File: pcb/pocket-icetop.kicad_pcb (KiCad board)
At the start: 2 copper layers, 100 x 50 mm, 39 parts, among them CON1 5V_DC, P1 USB_B, P2 LED_POWER, P3 ICSP, P4 LED_STRIP, SW1 RESET, SW2 SW_DEMO1, SW3 SW_DEMO2, U1 ATMEGA32U4-A, Y1 Crystal

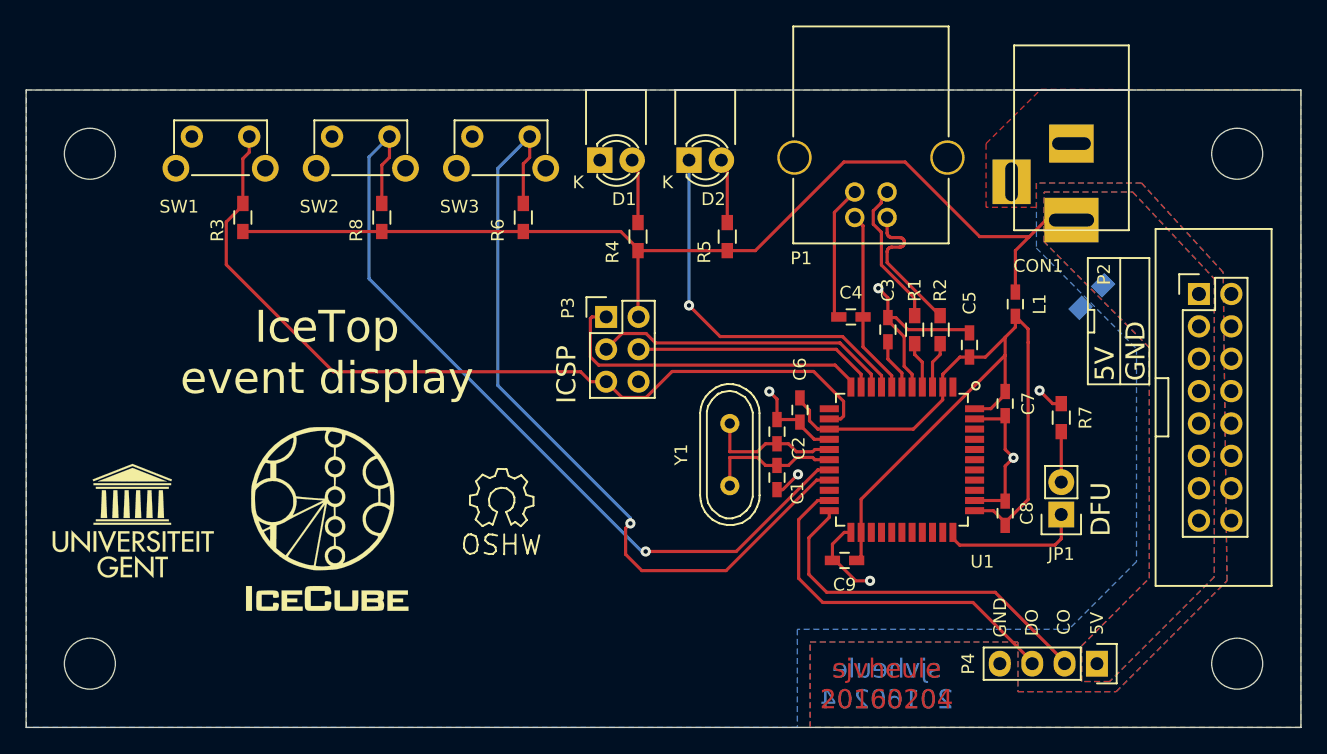
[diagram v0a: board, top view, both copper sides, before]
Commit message: Drop DFU jumper by using SW3 as dual-purpose input: demo button and DFU select during reset.
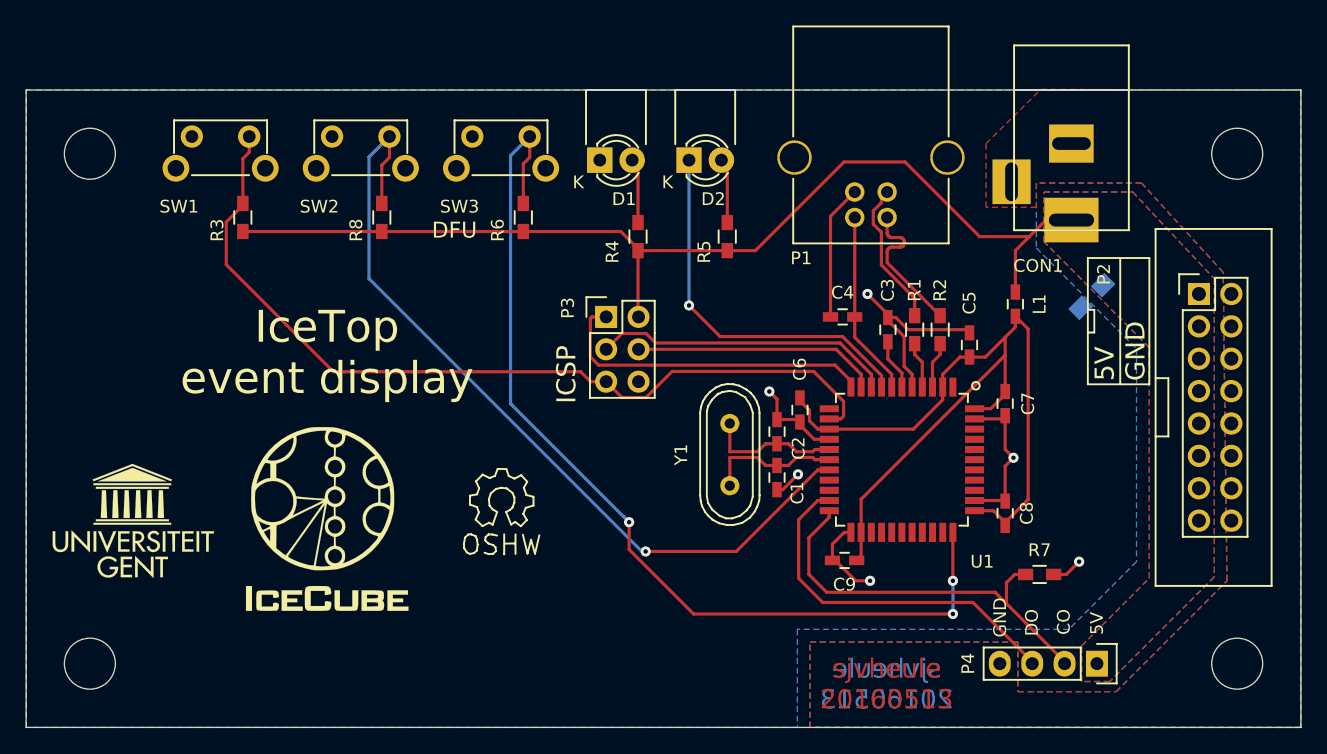
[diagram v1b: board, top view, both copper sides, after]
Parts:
- removed JP1: JUMPER, Pin_Headers:Pin_Header_Straight_1x02
- C1, C2: value 6p -> 6.8p
- U1: value ATMEGA32U4-A -> ATMEGA32U4-AU
- moved R7 12.4 mm to (121.5, 80.0), turned to 0 degrees
- moved C4 0.65 mm to (106.0, 59.8)
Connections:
- R7 pad 1: GND -> LED_clk
- R7 pad 2: Net-(JP1-Pad2) -> GND
- U1 pad 19: /DEMO2 -> Net-(U1-Pad19)
- U1 pad 33: Net-(JP1-Pad1) -> /DEMO2
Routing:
- net /DEMO2: track 63.2 -> 76.7 mm, vias 1 -> 3
- net Net-(JP1-Pad1): track 11.3 -> 0.00 mm
- net Net-(JP1-Pad2): track 3.96 -> 0.00 mm
- net LED_clk: track 28.7 -> 32.1 mm
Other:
- board text added: "Rev 2: Update DC jack footprint, move copper fills accordingly Rev 3: Move C4 to make room for C3's marking by moving C3's GND via Add pull-down to LED clock line Replace DFU jumper by SW3"
- board text added: "sjvheule 20160513"
- board text removed: "Rev 2: Update DC jack footprint, move copper fills accordingly"
- board text removed: "sjvheule 20160204"
